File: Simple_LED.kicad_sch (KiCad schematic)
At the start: 2 parts

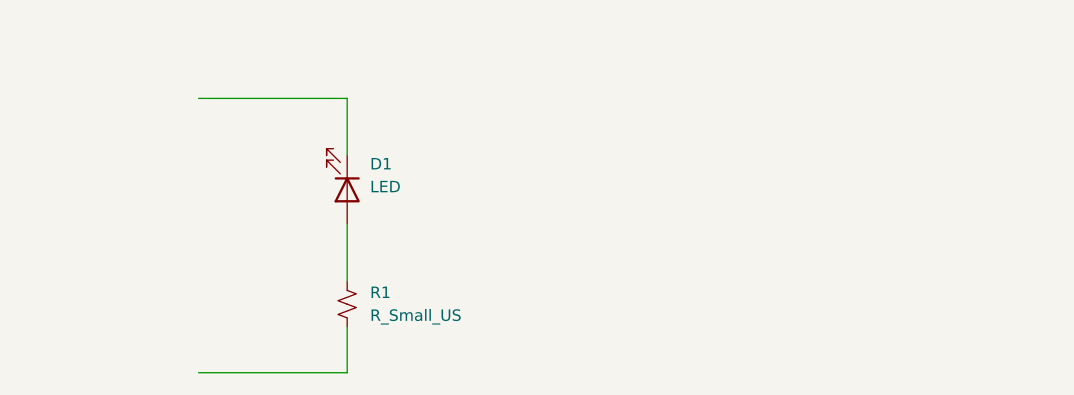
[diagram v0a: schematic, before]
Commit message: Switch added to schematic
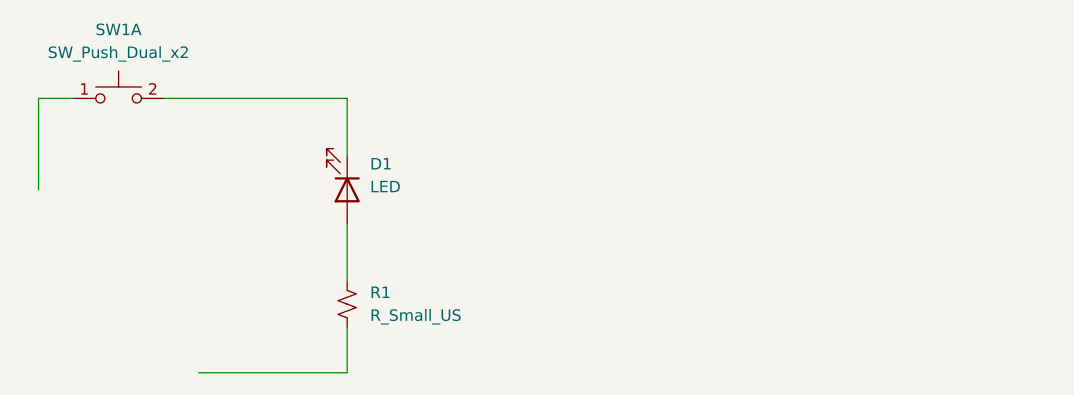
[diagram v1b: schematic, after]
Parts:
- added SW1: SW_Push_Dual_x2, symbol Switch:SW_Push_Dual_x2
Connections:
- net at D1.1 (K): now also SW1.2 (D)
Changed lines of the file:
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@@
 	(wire
 		(pts
-			(xy 63.5 68.58) (xy 80.01 68.58)
+			(xy 80.01 93.98) (xy 80.01 99.06)
 		)
 		(stroke
@@
 	(wire
 		(pts
-			(xy 80.01 93.98) (xy 80.01 99.06)
+			(xy 59.69 68.58) (xy 80.01 68.58)
 		)
 		(stroke
@@
 	(wire
 		(pts
+			(xy 49.53 68.58) (xy 45.72 68.58)
+		)
+		(stroke
+			(width 0)
+			(type default)
+		)
+	)
+	(wire
+		(pts
 			(xy 63.5 99.06) (xy 80.01 99.06)
 		)
@@
 		)
 	)
+	(wire
+		(pts
+			(xy 45.72 68.58) (xy 45.72 78.74)
+		)
+		(stroke
+			(width 0)
+			(type default)
+		)
+	)
+	(symbol
+		(lib_id "Switch:SW_Push_Dual_x2")
+		(at 54.61 68.58 0)
+		(unit 1)
+		(exclude_from_sim no)
+		(in_bom yes)
+		(on_board yes)
+		(dnp no)
+		(fields_autoplaced yes)
+		(property "Reference" "SW1"
+			(at 54.61 60.96 0)
+			(effects
+				(font
+					(size 1.27 1.27)
+				)
+			)
+		)
+		(property "Value" "SW_Push_Dual_x2"
+			(at 54.61 63.5 0)
+			(effects
+				(font
+					(size 1.27 1.27)
+				)
+			)
+		)
+		(property "Footprint" ""
+			(at 54.61 63.5 0)
+			(effects
+				(font
+					(size 1.27 1.27)
+				)
+				(hide yes)
+			)
+		)
+		(property "Datasheet" "~"
+			(at 54.61 63.5 0)
+			(effects
+				(font
+					(size 1.27 1.27)
+				)
+				(hide yes)
+			)
+		)
+		(property "Description" "Push button switch, generic, separate symbols, four pins"
+			(at 54.61 68.58 0)
+			(effects
+				(font
+					(size 1.27 1.27)
+				)
+				(hide yes)
+			)
+		)
+		(pin "2"
+		)
+		(pin "1"
+		)
+		(pin "3"
+		)
+		(pin "4"
+		)
+		(instances
+			(project "Simple_LED"
+				(path "/5bb29c81-3bb8-4c79-8b92-0b92f90eac6b"
+					(reference "SW1")
+					(unit 1)
+				)
+			)
+		)
+	)

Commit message: Battery added to schematic
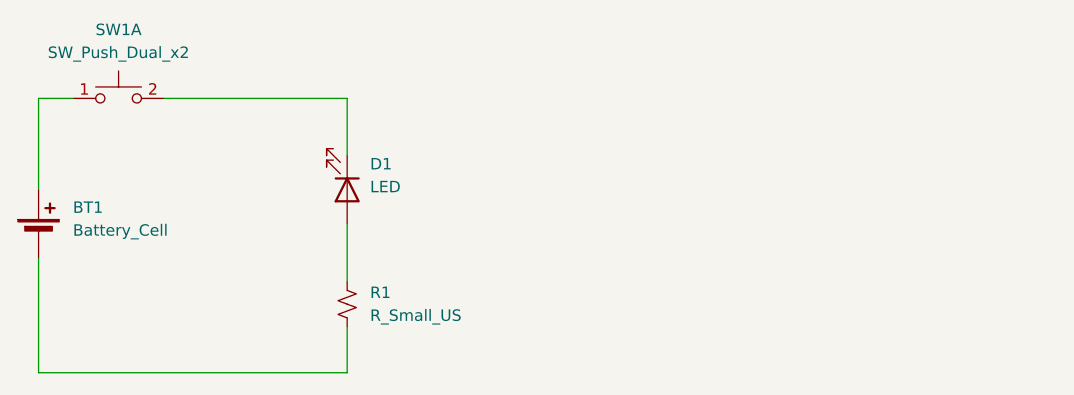
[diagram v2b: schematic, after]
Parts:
- added BT1: Battery_Cell, symbol Device:Battery_Cell
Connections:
- net at SW1.1 (C): now also BT1.1 (+)
- net at R1.2: now also BT1.2 (-)
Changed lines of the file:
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@@
+	(wire
+		(pts
+			(xy 45.72 99.06) (xy 80.01 99.06)
+		)
+		(stroke
+			(width 0)
+			(type default)
+		)
+	)
 	(wire
 		(pts
 			(xy 80.01 93.98) (xy 80.01 99.06)
+		)
+		(stroke
+			(width 0)
+			(type default)
+		)
+	)
+	(wire
+		(pts
+			(xy 45.72 99.06) (xy 45.72 86.36)
 		)
 		(stroke
@@
 		(pts
 			(xy 49.53 68.58) (xy 45.72 68.58)
-		)
-		(stroke
-			(width 0)
-			(type default)
-		)
-	)
-	(wire
-		(pts
-			(xy 63.5 99.06) (xy 80.01 99.06)
 		)
 		(stroke
@@
 					(unit 1)
 				)
+			)
+		)
+	)
+	(symbol
+		(lib_id "Device:Battery_Cell")
+		(at 45.72 83.82 0)
+		(unit 1)
+		(exclude_from_sim no)
+		(in_bom yes)
+		(on_board yes)
+		(dnp no)
+		(fields_autoplaced yes)
+		(property "Reference" "BT1"
+			(at 49.53 80.7084 0)
+			(effects
+				(font
+					(size 1.27 1.27)
+				)
+				(justify left)
+			)
+		)
+		(property "Value" "Battery_Cell"
+			(at 49.53 83.2484 0)
+			(effects
+				(font
+					(size 1.27 1.27)
+				)
+				(justify left)
+			)
+		)
+		(property "Footprint" ""
+			(at 45.72 82.296 90)
+			(effects
+				(font
+					(size 1.27 1.27)
+				)
+				(hide yes)
+			)
+		)
+		(property "Datasheet" "~"
+			(at 45.72 82.296 90)
+			(effects
+				(font
+					(size 1.27 1.27)
+				)
+				(hide yes)
+			)
+		)
+		(property "Description" "Single-cell battery"
+			(at 45.72 83.82 0)
+			(effects
+				(font
+					(size 1.27 1.27)
+				)
+				(hide yes)
+			)
+		)
+		(pin "2"
+		)
+		(pin "1"
+		)
+		(instances
+			(project "Simple_LED"
+				(path "/5bb29c81-3bb8-4c79-8b92-0b92f90eac6b"
+					(reference "BT1")
+					(unit 1)
+				)

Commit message: 2nd LED and resistor added
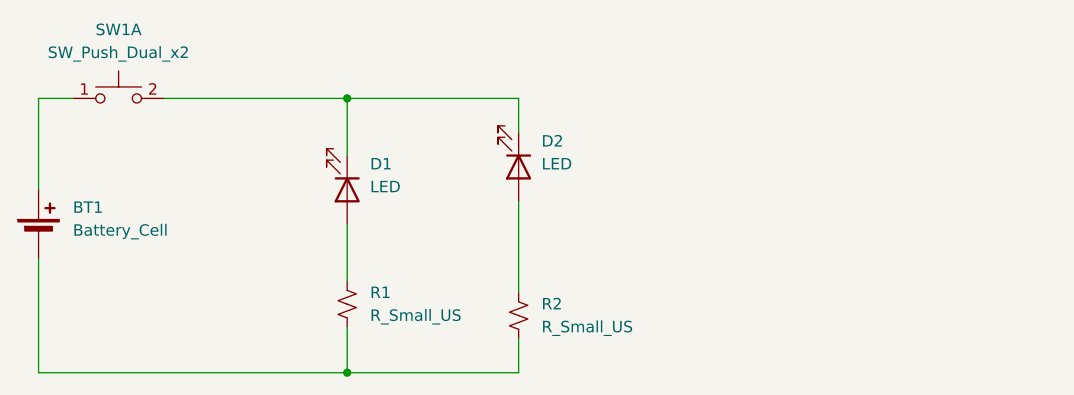
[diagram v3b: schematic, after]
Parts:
- added D2: LED, LED_SMD:LED_0402_1005Metric, symbol Device:LED
- added R2: R_Small_US, Resistor_SMD:R_0402_1005Metric, symbol Device:R_Small_US
- D1: footprint (none) -> LED_SMD:LED_0402_1005Metric
- R1: footprint (none) -> Resistor_SMD:R_0402_1005Metric
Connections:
- net at D1.1 (K), SW1.2 (D): now also D2.1 (K)
- net at BT1.2 (-), R1.2: now also R2.2
- new net: D2.2 (A), R2.1
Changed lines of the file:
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@@
 	(generator_version "8.0")
 	(paper "A4")
+	(junction
+		(at 80.01 68.58)
+		(diameter 0)
+		(color 0 0 0 0)
+	)
+	(junction
+		(at 80.01 99.06)
+		(diameter 0)
+		(color 0 0 0 0)
+	)
 	(wire
 		(pts
@@
 	(wire
 		(pts
+			(xy 99.06 68.58) (xy 80.01 68.58)
+		)
+		(stroke
+			(width 0)
+			(type default)
+		)
+	)
+	(wire
+		(pts
 			(xy 80.01 93.98) (xy 80.01 99.06)
 		)
@@
 	(wire
 		(pts
+			(xy 99.06 80.01) (xy 99.06 90.17)
+		)
+		(stroke
+			(width 0)
+			(type default)
+		)
+	)
+	(wire
+		(pts
 			(xy 59.69 68.58) (xy 80.01 68.58)
 		)
@@
 	(wire
 		(pts
+			(xy 80.01 99.06) (xy 99.06 99.06)
+		)
+		(stroke
+			(width 0)
+			(type default)
+		)
+	)
+	(wire
+		(pts
+			(xy 99.06 95.25) (xy 99.06 99.06)
+		)
+		(stroke
+			(width 0)
+			(type default)
+		)
+	)
+	(wire
+		(pts
 			(xy 45.72 68.58) (xy 45.72 78.74)
 		)
@@
 			(width 0)
 			(type default)
+		)
+	)
+	(wire
+		(pts
+			(xy 99.06 72.39) (xy 99.06 68.58)
+		)
+		(stroke
+			(width 0)
+			(type default)
+		)
+	)
+	(symbol
+		(lib_id "Device:LED")
+		(at 99.06 76.2 270)
+		(unit 1)
+		(exclude_from_sim no)
+		(in_bom yes)
+		(on_board yes)
+		(dnp no)
+		(fields_autoplaced yes)
+		(property "Reference" "D2"
+			(at 101.6 73.3424 90)
+			(effects
+				(font
+					(size 1.27 1.27)
+				)
+				(justify left)
+			)
+		)
+		(property "Value" "LED"
+			(at 101.6 75.8824 90)
+			(effects
+				(font
+					(size 1.27 1.27)
+				)
+				(justify left)
+			)
+		)
+		(property "Footprint" "LED_SMD:LED_0402_1005Metric"
+			(at 99.06 76.2 0)
+			(effects
+				(font
+					(size 1.27 1.27)
+				)
+				(hide yes)
+			)
+		)
+		(property "Datasheet" "~"
+			(at 99.06 76.2 0)
+			(effects
+				(font
+					(size 1.27 1.27)
+				)
+				(hide yes)
+			)
+		)
+		(property "Description" "Light emitting diode"
+			(at 99.06 76.2 0)
+			(effects
+				(font
+					(size 1.27 1.27)
+				)
+				(hide yes)
+			)
+		)
+		(pin "1"
+		)
+		(pin "2"
+		)
+		(instances
+			(project "Simple_LED"
+				(path "/5bb29c81-3bb8-4c79-8b92-0b92f90eac6b"
+					(reference "D2")
+					(unit 1)
+				)
+			)
 		)
 	)
@@
 	(symbol
 		(lib_id "Device:R_Small_US")
+		(at 99.06 92.71 0)
+		(unit 1)
+		(exclude_from_sim no)
+		(in_bom yes)
+		(on_board yes)
+		(dnp no)
+		(fields_autoplaced yes)
+		(property "Reference" "R2"
+			(at 101.6 91.4399 0)
+			(effects
+				(font
+					(size 1.27 1.27)
+				)
+				(justify left)
+			)
+		)
+		(property "Value" "R_Small_US"
+			(at 101.6 93.9799 0)
+			(effects
+				(font
+					(size 1.27 1.27)
+				)
+				(justify left)
+			)
+		)
+		(property "Footprint" "Resistor_SMD:R_0402_1005Metric"
+			(at 99.06 92.71 0)
+			(effects
+				(font
+					(size 1.27 1.27)
+				)
+				(hide yes)
+			)
+		)
+		(property "Datasheet" "~"
+			(at 99.06 92.71 0)
+			(effects
+				(font
+					(size 1.27 1.27)
+				)
+				(hide yes)
+			)
+		)
+		(property "Description" "Resistor, small US symbol"
+			(at 99.06 92.71 0)
+			(effects
+				(font
+					(size 1.27 1.27)
+				)
+				(hide yes)
+			)
+		)
+		(pin "2"
+		)
+		(pin "1"
+		)
+		(instances
+			(project "Simple_LED"
+				(path "/5bb29c81-3bb8-4c79-8b92-0b92f90eac6b"
+					(reference "R2")
+					(unit 1)
+				)
+			)
+		)
+	)
+	(symbol
+		(lib_id "Device:R_Small_US")
 		(at 80.01 91.44 0)
 		(unit 1)
@@
 			)
 		)
-		(property "Footprint" ""
+		(property "Footprint" "Resistor_SMD:R_0402_1005Metric"
 			(at 80.01 91.44 0)
 			(effects
@@
 			)
 		)
-		(property "Footprint" ""
+		(property "Footprint" "LED_SMD:LED_0402_1005Metric"
 			(at 80.01 78.74 0)
 			(effects

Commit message: created SMD PCB
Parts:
- BT1: footprint (none) -> Battery:BatteryHolder_Keystone_1060_1x2032
- SW1: footprint (none) -> Button_Switch_SMD:SW_Push_1P1T_NO_6x6mm_H9.5mm
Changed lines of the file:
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@@
 			)
 		)
-		(property "Footprint" ""
+		(property "Footprint" "Button_Switch_SMD:SW_Push_1P1T_NO_6x6mm_H9.5mm"
 			(at 54.61 63.5 0)
 			(effects
@@
 			)
 		)
-		(property "Footprint" ""
+		(property "Footprint" "Battery:BatteryHolder_Keystone_1060_1x2032"
 			(at 45.72 82.296 90)
 			(effects

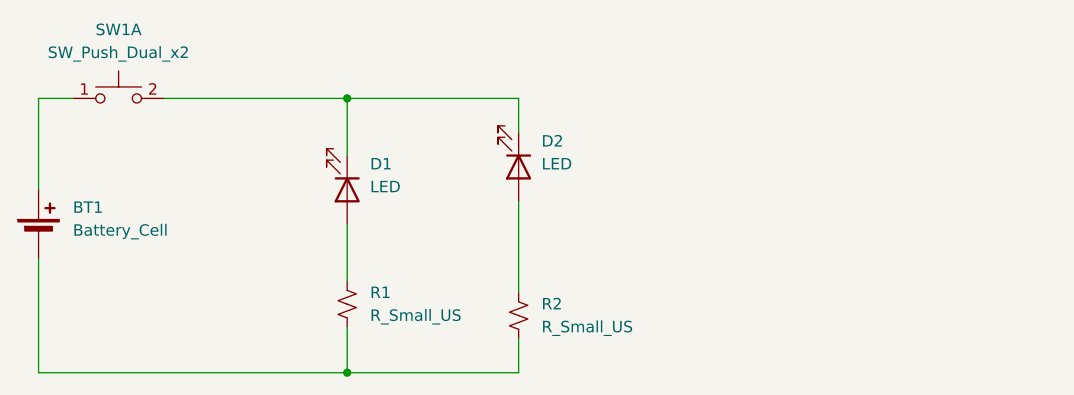
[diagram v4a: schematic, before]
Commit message: added soundskrit_skr04xx symbol and footprint
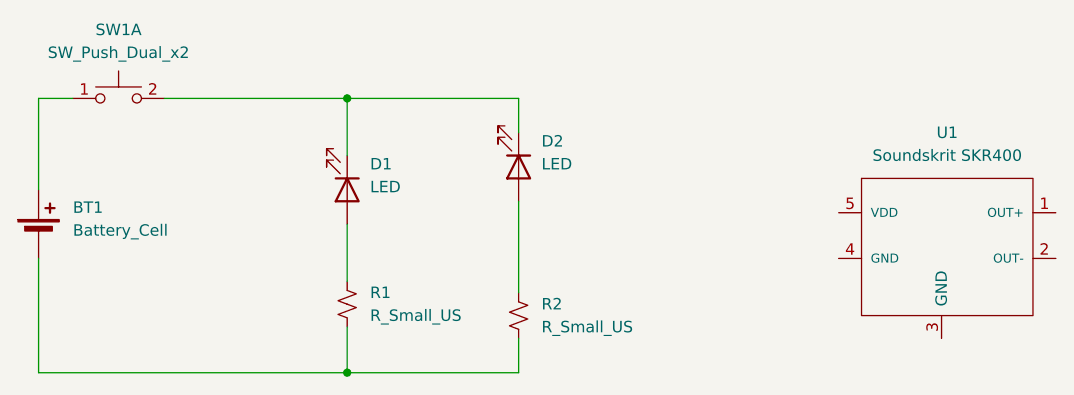
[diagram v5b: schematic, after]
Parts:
- added U1: Soundskrit SKR400, soundskrit_skr04xx:soundskrit_skr4xx_v2402, symbol soundskrit_skr04xx:soundskrit_skr400_v1.0
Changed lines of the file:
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@@
+	)
+	(symbol
+		(lib_id "soundskrit_skr04xx:soundskrit_skr400_v1.0")
+		(at 140.97 76.2 0)
+		(unit 1)
+		(exclude_from_sim no)
+		(in_bom yes)
+		(on_board yes)
+		(dnp no)
+		(fields_autoplaced yes)
+		(property "Reference" "U1"
+			(at 146.685 72.39 0)
+			(effects
+				(font
+					(size 1.27 1.27)
+				)
+			)
+		)
+		(property "Value" "Soundskrit SKR400"
+			(at 146.685 74.93 0)
+			(effects
+				(font
+					(size 1.27 1.27)
+				)
+			)
+		)
+		(property "Footprint" "soundskrit_skr04xx:soundskrit_skr4xx_v2402"
+			(at 165.1 106.68 0)
+			(effects
+				(font
+					(size 1.27 1.27)
+				)
+				(hide yes)
+			)
+		)
+		(property "Datasheet" ""
+			(at 140.97 76.2 0)
+			(effects
+				(font
+					(size 1.27 1.27)
+				)
+				(hide yes)
+			)
+		)
+		(property "Description" "Soundskrit Analog microphone"
+			(at 140.97 76.2 0)
+			(effects
+				(font
+					(size 1.27 1.27)
+				)
+				(hide yes)
+			)
+		)
+		(pin "3"
+		)
+		(pin "5"
+		)
+		(pin "2"
+		)
+		(pin "4"
+		)
+		(pin "1"
+		)
+		(instances
+			(project "Simple_LED"
+				(path "/5bb29c81-3bb8-4c79-8b92-0b92f90eac6b"
+					(reference "U1")
+					(unit 1)
+				)
+			)
+		)
 	)
 	(symbol
